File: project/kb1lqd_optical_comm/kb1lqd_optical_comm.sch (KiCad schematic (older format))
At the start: 13 parts

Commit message: Schematic essentially done.
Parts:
- removed J? (x2): 0022052021, symbol kb1lqd_optical_comm:0022052021
- added J4: Conn_01x04_Male, symbol Connector:Conn_01x04_Male
- added J5: Conn_01x02_Male, symbol Connector:Conn_01x02_Male
- added J6: SJ1-3523N, symbol kb1lqd_optical_comm:SJ1-3523N
- added R2, R6, R7: 10k, symbol Device:R_US
- added R?: 0, symbol Device:R_US
- D1: renamed from D?; value LED -> VLCS5830
- gave numbers to parts that had none: 10
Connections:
- net labels added: AUDIO_OUT1, AUDIO_OUT2
- wire segments 43 -> 65
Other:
- note added: "1/8" Jack Line Input"
- note added: "2.5mm Connector\nTip = Speaker+\nRing = Unused\nShield = GND"
- note added: "3.5mm Connector\nTip = AUDIO1\nRing = AUDIO2\nShield = GND\nSJ1-3523N"
- note added: "3.5mm Connector\nTip = V+\nRing = Mic+\nShield = Mic-"
- note added: "AUX 1/8" Output Audio"
- note added: "EXTRA AUDIO INPUT"
- note added: "EXTRA AUDIO OUTPUT"
- note added: "Kenwood Style Audio Jack"
- note removed: "2.5mm Connector\nTip = Speaker+\nRing = Unused\nShield = GND (Speaker-)\nSJ1-2503A"
- note removed: "3.5mm Connector\nTip = V+\nRing = Mic+\nShield = Mic-\nSJ1-3523N"
- moved on the sheet: D1, R3, R4, SW3

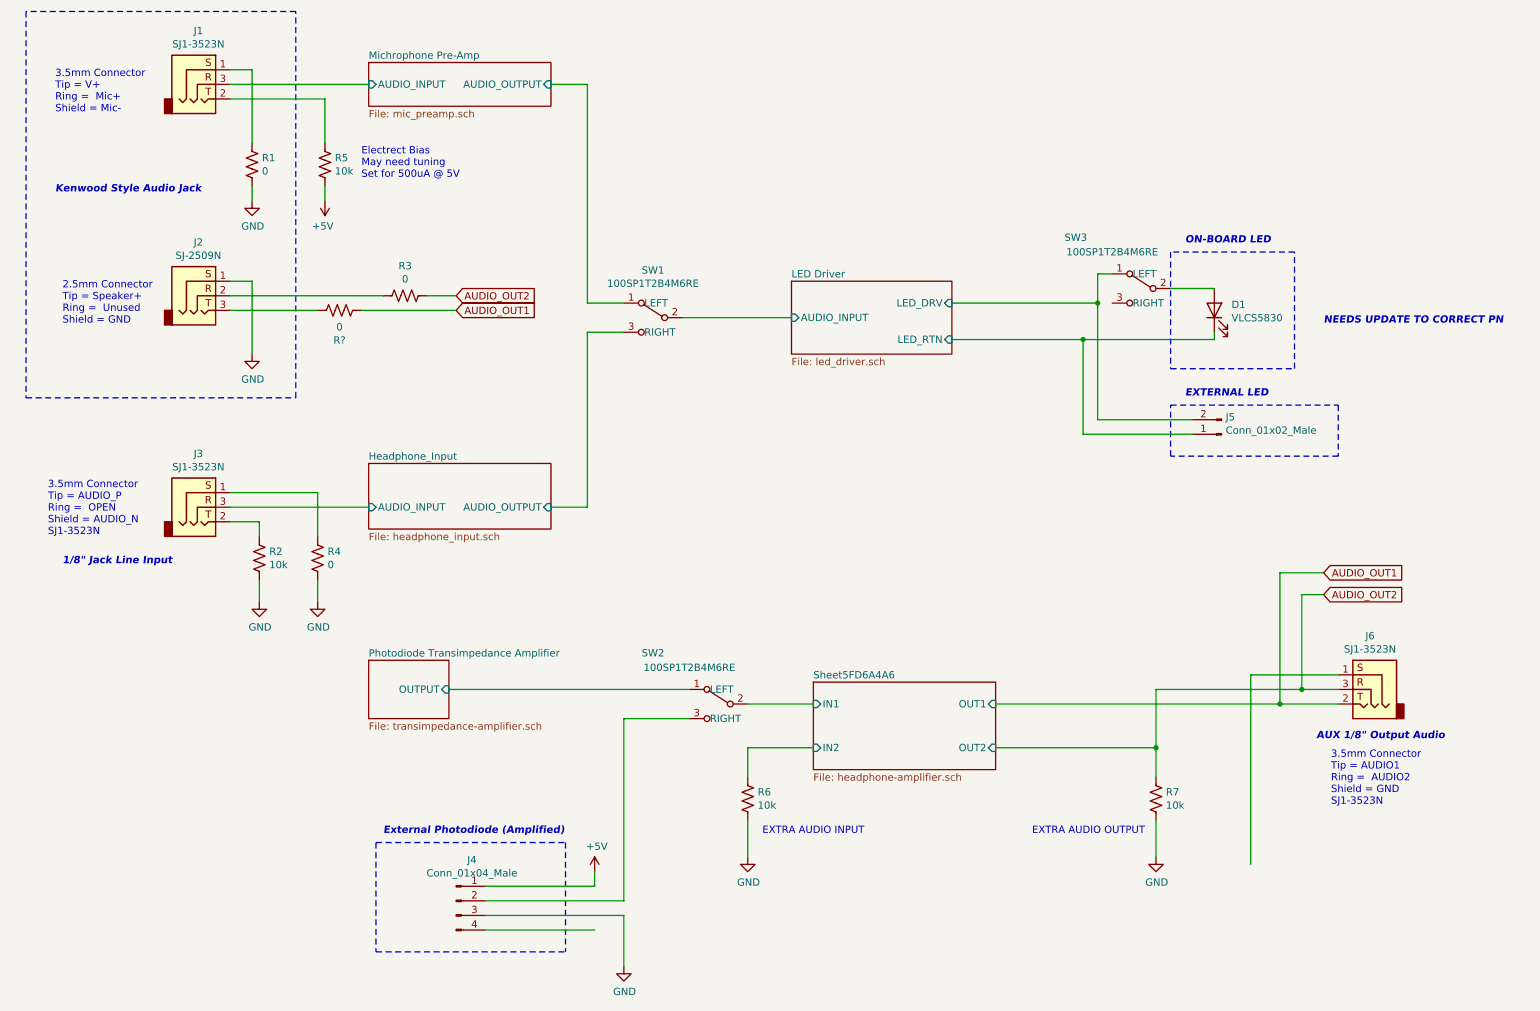
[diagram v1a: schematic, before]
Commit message: Fixing ERC errors.
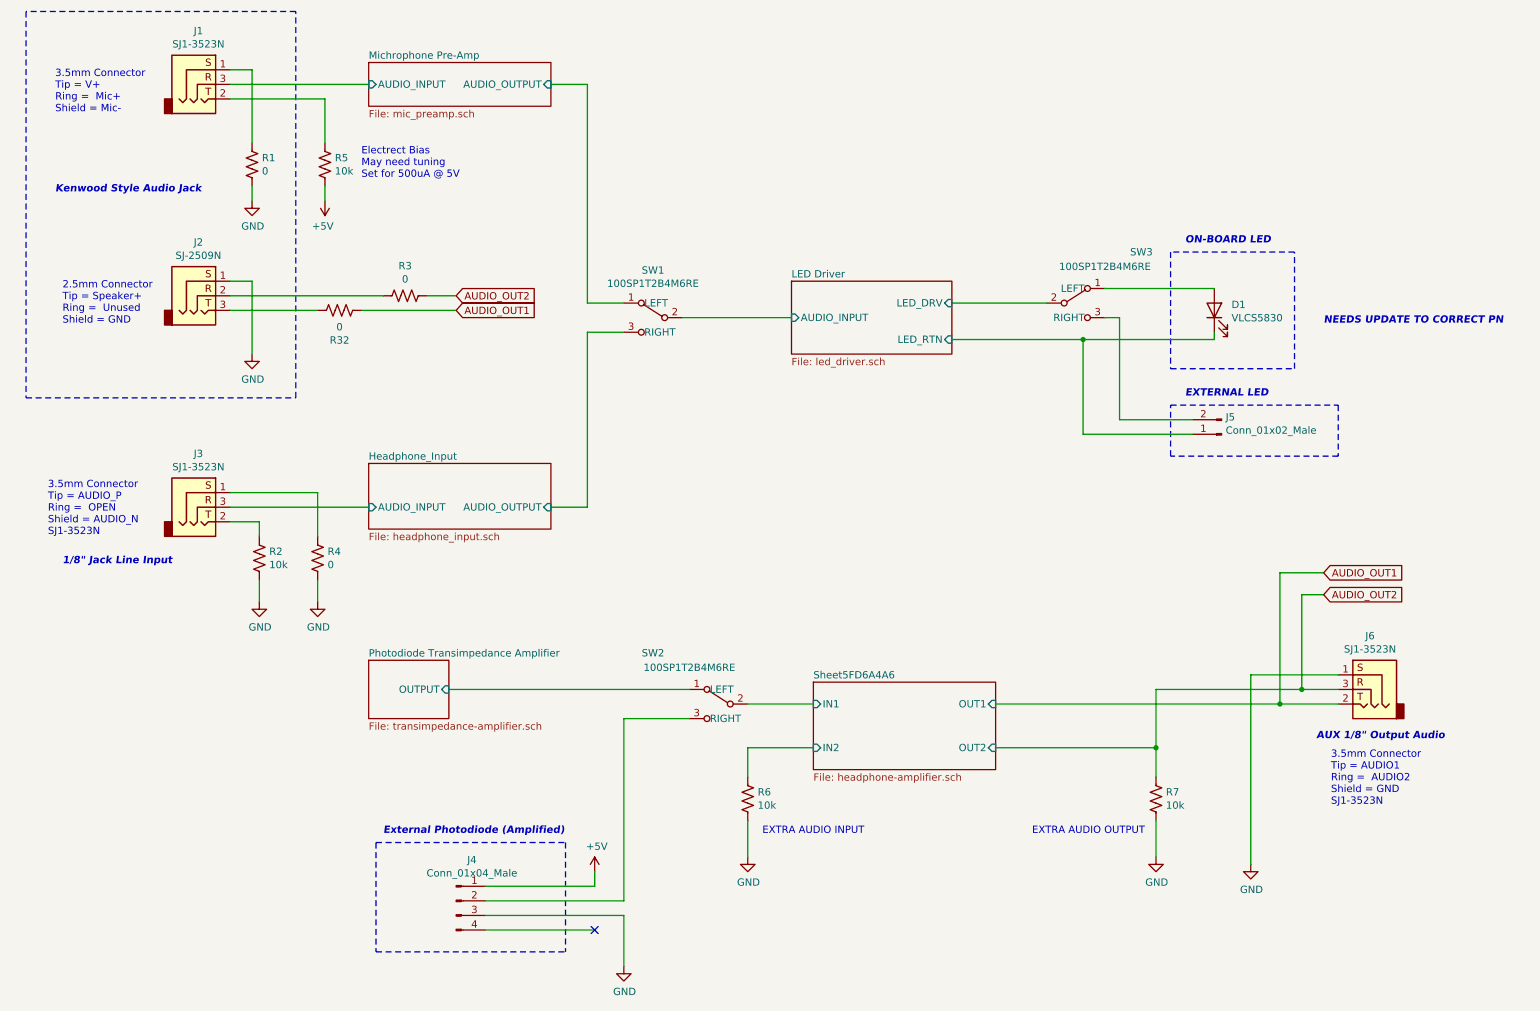
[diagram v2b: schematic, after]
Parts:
- gave numbers to parts that had none: 1
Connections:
- wire segments 65 -> 64
- no-connect marks 0 -> 1
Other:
- moved on the sheet: SW3
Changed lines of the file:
@@
 	7900 3600 8650 3600
 Wire Wire Line
-	7000 2700 8000 2700
-Wire Wire Line
-	8000 2700 8000 3500
-Wire Wire Line
-	8000 3500 8650 3500
+	7000 2700 7650 2700
 Text Notes 850  1400 0    50   ~ 0
 3.5mm Connector\nTip = V+\nRing =  Mic+\nShield = Mic-
@@
 	-1   0    0    -1
 $EndComp
-Wire Wire Line
-	8100 2500 8000 2500
-Wire Wire Line
-	8000 2500 8000 2700
-Connection ~ 8000 2700
 $Comp
 L kb1lqd_optical_comm:100SP1T2B4M6RE SW3
 U 1 1 5F759014
-P 8750 2750
-F 0 "SW3" H 9650 3250 50  0000 C CNN
-F 1 "100SP1T2B4M6RE" H 9400 3150 50  0000 C CNN
-F 2 "" H 8750 2750 50  0001 C CNN
-F 3 "" H 8750 2750 50  0001 C CNN
-	1    8750 2750
-	-1   0    0    -1
+P 7400 2850
+F 0 "SW3" H 8300 3350 50  0000 C CNN
+F 1 "100SP1T2B4M6RE" H 8050 3250 50  0000 C CNN
+F 2 "" H 7400 2850 50  0001 C CNN
+F 3 "" H 7400 2850 50  0001 C CNN
+	1    7400 2850
+	1    0    0    -1
 $EndComp
 $Comp
@@
 	3800 6900 4750 6900
 $Comp
-L power:GND #PWR?
+L power:GND #PWR0101
 U 1 1 5FDF4870
 P 4750 7250
-F 0 "#PWR?" H 4750 7000 50  0001 C CNN
+F 0 "#PWR0101" H 4750 7000 50  0001 C CNN
 F 1 "GND" H 4755 7077 50  0000 C CNN
 F 2 "" H 4750 7250 50  0001 C CNN
@@
 	3800 7000 4550 7000
 $Comp
-L power:+5V #PWR?
+L power:+5V #PWR0102
 U 1 1 5FDFB5DD
 P 4550 6600
-F 0 "#PWR?" H 4550 6450 50  0001 C CNN
+F 0 "#PWR0102" H 4550 6450 50  0001 C CNN
 F 1 "+5V" H 4565 6773 50  0000 C CNN
 F 2 "" H 4550 6600 50  0001 C CNN
@@
 AUDIO_OUT2
 $Comp
-L Device:R_US R?
+L Device:R_US R32
 U 1 1 5FE25BFA
 P 2800 2750
-F 0 "R?" V 2595 2750 50  0000 C CNN
+F 0 "R32" V 2595 2750 50  0000 C CNN
 F 1 "0" V 2686 2750 50  0000 C CNN
 F 2 "" V 2840 2740 50  0001 C CNN
@@
 Wire Wire Line
 	7900 2950 8800 2950
-Wire Wire Line
-	8500 2600 8800 2600
 Wire Wire Line
 	8800 2950 8800 2900
@@
 Wire Wire Line
 	3550 5350 5200 5350
+NoConn ~ 4550 7000
+$Comp
+L power:GND #PWR0105
+U 1 1 5FE7F1D6
+P 9050 6550
+F 0 "#PWR0105" H 9050 6300 50  0001 C CNN
+F 1 "GND" H 9055 6377 50  0000 C CNN
+F 2 "" H 9050 6550 50  0001 C CNN
+F 3 "" H 9050 6550 50  0001 C CNN
+	1    9050 6550
+	1    0    0    -1
+$EndComp
+Wire Wire Line
+	8050 2600 8800 2600
+Wire Wire Line
+	8050 2800 8150 2800
+Wire Wire Line
+	8150 2800 8150 3500
+Wire Wire Line
+	8150 3500 8650 3500
 $EndSCHEMATC

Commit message: Updated with all footprints
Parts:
- removed J1, J3, J6: SJ1-3523N, symbol kb1lqd_optical_comm:SJ1-3523N
- removed J2: SJ-2509N, symbol kb1lqd_optical_comm:SJ-2509N
- removed SW1, SW2, SW3: 100SP1T2B4M6RE, symbol kb1lqd_optical_comm:100SP1T2B4M6RE
- added J1, J3, J6: SJ1-3523N, SJ1-3523N:CUI_SJ1-3523N, symbol SJ1-3523N:SJ1-3523N
- added J2: SJ-2509N, SJ-2509N (1):CUI_SJ-2509N, symbol SJ-2509N:SJ-2509N
- added SW1, SW2, SW3: EG1213, EG1213:SW_EG1213, symbol EG1213:EG1213
- D1: footprint (none) -> LED_THT:LED_D5.0mm
- J4: footprint (none) -> Connector_Molex:Molex_KK-254_AE-6410-04A_1x04_P2.54mm_Vertical
- J5: footprint (none) -> Connector_Molex:Molex_KK-254_AE-6410-02A_1x02_P2.54mm_Vertical
- R1, R2, R3, R32, R4, R5, R6, R7: footprint (none) -> Resistor_SMD:R_0603_1608Metric
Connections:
- net AUDIO_OUT1: now also J6.2
- net AUDIO_OUT2: now also J6.3
- net GND: now also J2.1, J6.1
- net Headphone_Input/AUDIO_INPUT: now also J3.3
- net Headphone_Input/AUDIO_OUTPUT: now also SW1.3
- net LED Driver/AUDIO_INPUT: now also SW1.2
- net LED Driver/LED_DRV: now also SW3.2
- net Michrophone Pre-Amp/AUDIO_INPUT: now also J1.3
- net Michrophone Pre-Amp/AUDIO_OUTPUT: now also SW1.1
- net Photodiode Transimpedance Amplifier/OUTPUT: now also SW2.1
- net Sheet5FD6A4A6/IN1: now also SW2.2
- net at D1.2 (A): now also SW3.3
- net at R1.1: now also J1.1
- net at R5.1: now also J1.2
- net at R3.2: now also J2.2
- net at R32.1: now also J2.3
- net at J5.2 (Pin_2): now also SW3.1
- net at J4.2 (Pin_2): now also SW2.3
- net at R4.1: now also J3.1
- net at R2.1: now also J3.2

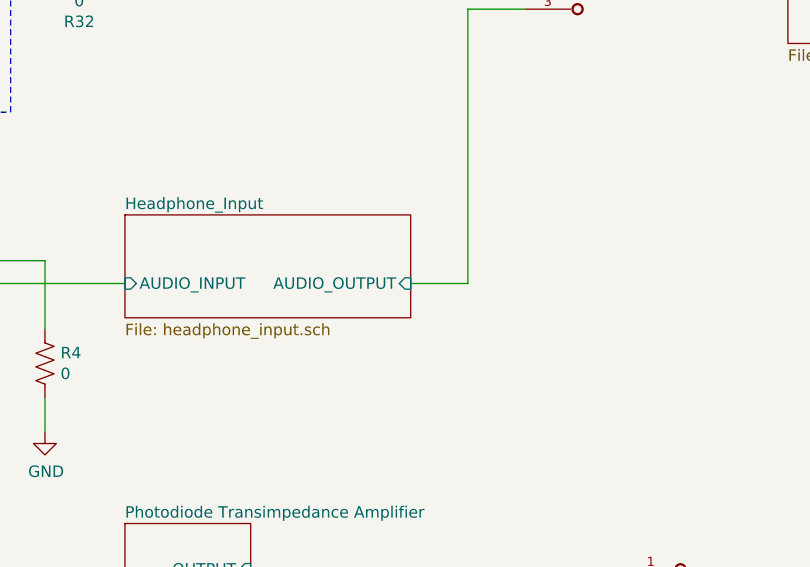
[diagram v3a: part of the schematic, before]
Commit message: Initial placement condensed.
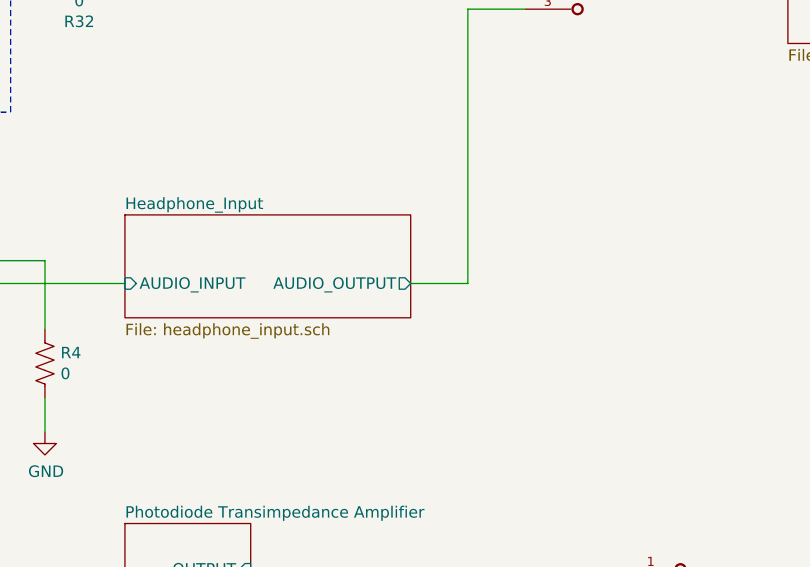
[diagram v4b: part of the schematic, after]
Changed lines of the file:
@@
 F0 "Headphone_Input" 50
 F1 "headphone_input.sch" 50
-F2 "AUDIO_OUTPUT" I R 4250 4100 50
+F2 "AUDIO_OUTPUT" O R 4250 4100 50
 F3 "AUDIO_INPUT" I L 3000 4100 50
 $EndSheet

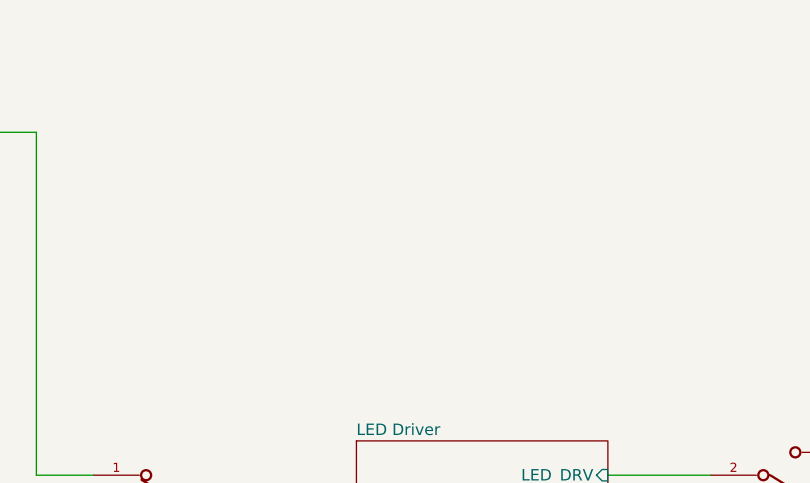
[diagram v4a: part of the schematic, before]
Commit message: More placement. Ready for board outline update.
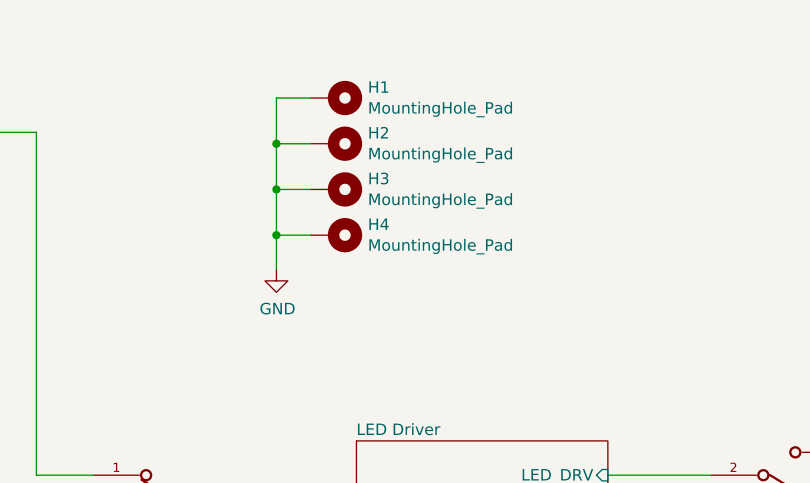
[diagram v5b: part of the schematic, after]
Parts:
- added H1, H2, H3, H4: MountingHole_Pad, MountingHole:MountingHole_4.3mm_M4, symbol Mechanical:MountingHole_Pad
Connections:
- net GND: now also H1.1, H2.1, H3.1, H4.1
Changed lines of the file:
@@
 Wire Wire Line
 	8800 4550 8600 4550
+$Comp
+L Mechanical:MountingHole_Pad H1
+U 1 1 5FEF8BB0
+P 5800 1050
+F 0 "H1" V 5754 1200 50  0000 L CNN
+F 1 "MountingHole_Pad" V 5845 1200 50  0000 L CNN
+F 2 "MountingHole:MountingHole_4.3mm_M4" H 5800 1050 50  0001 C CNN
+F 3 "~" H 5800 1050 50  0001 C CNN
+	1    5800 1050
+	0    1    1    0
+$EndComp
+$Comp
+L Mechanical:MountingHole_Pad H2
+U 1 1 5FEFB20E
+P 5800 1250
+F 0 "H2" V 5754 1400 50  0000 L CNN
+F 1 "MountingHole_Pad" V 5845 1400 50  0000 L CNN
+F 2 "MountingHole:MountingHole_4.3mm_M4" H 5800 1250 50  0001 C CNN
+F 3 "~" H 5800 1250 50  0001 C CNN
+	1    5800 1250
+	0    1    1    0
+$EndComp
+$Comp
+L Mechanical:MountingHole_Pad H3
+U 1 1 5FEFB438
+P 5800 1450
+F 0 "H3" V 5754 1600 50  0000 L CNN
+F 1 "MountingHole_Pad" V 5845 1600 50  0000 L CNN
+F 2 "MountingHole:MountingHole_4.3mm_M4" H 5800 1450 50  0001 C CNN
+F 3 "~" H 5800 1450 50  0001 C CNN
+	1    5800 1450
+	0    1    1    0
+$EndComp
+$Comp
+L Mechanical:MountingHole_Pad H4
+U 1 1 5FEFB6CC
+P 5800 1650
+F 0 "H4" V 5754 1800 50  0000 L CNN
+F 1 "MountingHole_Pad" V 5845 1800 50  0000 L CNN
+F 2 "MountingHole:MountingHole_4.3mm_M4" H 5800 1650 50  0001 C CNN
+F 3 "~" H 5800 1650 50  0001 C CNN
+	1    5800 1650
+	0    1    1    0
+$EndComp
+$Comp
+L power:GND #PWR039
+U 1 1 5FEFBEA6
+P 5550 1800
+F 0 "#PWR039" H 5550 1550 50  0001 C CNN
+F 1 "GND" H 5555 1627 50  0000 C CNN
+F 2 "" H 5550 1800 50  0001 C CNN
+F 3 "" H 5550 1800 50  0001 C CNN
+	1    5550 1800
+	1    0    0    -1
+$EndComp
+Wire Wire Line
+	5700 1050 5550 1050
+Wire Wire Line
+	5550 1050 5550 1250
+Wire Wire Line
+	5700 1650 5550 1650
+Connection ~ 5550 1650
+Wire Wire Line
+	5550 1650 5550 1800
+Wire Wire Line
+	5700 1450 5550 1450
+Connection ~ 5550 1450
+Wire Wire Line
+	5550 1450 5550 1650
+Wire Wire Line
+	5700 1250 5550 1250
+Connection ~ 5550 1250
+Wire Wire Line
+	5550 1250 5550 1450
 $EndSCHEMATC

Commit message: More.
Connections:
- net Headphone_Input/AUDIO_OUTPUT: now also SW1.1; no longer SW1.3
- net Michrophone Pre-Amp/AUDIO_OUTPUT: now also SW1.3; no longer SW1.1
- net Photodiode Transimpedance Amplifier/OUTPUT: now also SW2.3; no longer SW2.1
- net at D1.2 (A): now also SW3.1; no longer SW3.3
- net at J4.2 (Pin_2): now also SW2.1; no longer SW2.3
- net at J5.2 (Pin_2): now also SW3.3; no longer SW3.1
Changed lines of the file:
@@
 F 4 "E-Switch" H 5050 2800 50  0001 L BNN "MANUFACTURER"
 	1    5050 2800
-	1    0    0    -1
-$EndComp
-$Comp
-L EG1213:EG1213 SW2
-U 1 1 5FEA23A7
-P 5500 5450
-F 0 "SW2" H 5500 5450 50  0001 L BNN
-F 1 "EG1213" H 5500 5450 50  0001 L BNN
-F 2 "EG1213:SW_EG1213" H 5500 5450 50  0001 L BNN
-F 3 "" H 5500 5450 50  0001 L BNN
-F 4 "E-Switch" H 5500 5450 50  0001 L BNN "MANUFACTURER"
-	1    5500 5450
-	1    0    0    -1
+	1    0    0    1
 $EndComp
 Wire Wire Line
@@
 F 4 "E-Switch" H 7750 2700 50  0001 L BNN "MANUFACTURER"
 	1    7750 2700
-	-1   0    0    1
+	-1   0    0    -1
 $EndComp
 $Comp
@@
 Wire Wire Line
 	5550 1250 5550 1450
+$Comp
+L EG1213:EG1213 SW2
+U 1 1 5FEA23A7
+P 5500 5450
+F 0 "SW2" H 5500 5450 50  0001 L BNN
+F 1 "EG1213" H 5500 5450 50  0001 L BNN
+F 2 "EG1213:SW_EG1213" H 5500 5450 50  0001 L BNN
+F 3 "" H 5500 5450 50  0001 L BNN
+F 4 "E-Switch" H 5500 5450 50  0001 L BNN "MANUFACTURER"
+	1    5500 5450
+	1    0    0    1
+$EndComp
 $EndSCHEMATC

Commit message: Updated mounting holes. Created BOM.
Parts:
- H1, H2, H3, H4: footprint MountingHole:MountingHole_4.3mm_M4 -> MountingHole:MountingHole_4.3mm_M4_DIN965_Pad
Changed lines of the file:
@@
 F 0 "H1" V 5754 1200 50  0000 L CNN
 F 1 "MountingHole_Pad" V 5845 1200 50  0000 L CNN
-F 2 "MountingHole:MountingHole_4.3mm_M4" H 5800 1050 50  0001 C CNN
+F 2 "MountingHole:MountingHole_4.3mm_M4_DIN965_Pad" H 5800 1050 50  0001 C CNN
 F 3 "~" H 5800 1050 50  0001 C CNN
 	1    5800 1050
@@
 F 0 "H2" V 5754 1400 50  0000 L CNN
 F 1 "MountingHole_Pad" V 5845 1400 50  0000 L CNN
-F 2 "MountingHole:MountingHole_4.3mm_M4" H 5800 1250 50  0001 C CNN
+F 2 "MountingHole:MountingHole_4.3mm_M4_DIN965_Pad" H 5800 1250 50  0001 C CNN
 F 3 "~" H 5800 1250 50  0001 C CNN
 	1    5800 1250
@@
 F 0 "H3" V 5754 1600 50  0000 L CNN
 F 1 "MountingHole_Pad" V 5845 1600 50  0000 L CNN
-F 2 "MountingHole:MountingHole_4.3mm_M4" H 5800 1450 50  0001 C CNN
+F 2 "MountingHole:MountingHole_4.3mm_M4_DIN965_Pad" H 5800 1450 50  0001 C CNN
 F 3 "~" H 5800 1450 50  0001 C CNN
 	1    5800 1450
@@
 F 0 "H4" V 5754 1800 50  0000 L CNN
 F 1 "MountingHole_Pad" V 5845 1800 50  0000 L CNN
-F 2 "MountingHole:MountingHole_4.3mm_M4" H 5800 1650 50  0001 C CNN
+F 2 "MountingHole:MountingHole_4.3mm_M4_DIN965_Pad" H 5800 1650 50  0001 C CNN
 F 3 "~" H 5800 1650 50  0001 C CNN
 	1    5800 1650
